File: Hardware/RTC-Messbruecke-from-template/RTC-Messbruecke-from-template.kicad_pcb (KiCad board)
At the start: 2 copper layers, 68.6 x 53.3 mm, 43 parts, among them J1 Power, J2 Digital/PWM, J3 Analog, J4 Digital/PWM, J5 Conn_01x04, J6 Conn_01x04, J7 Conn_01x08, J8 Conn_01x04, U1 R-78E9.0-0.5, U3 MAX6105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

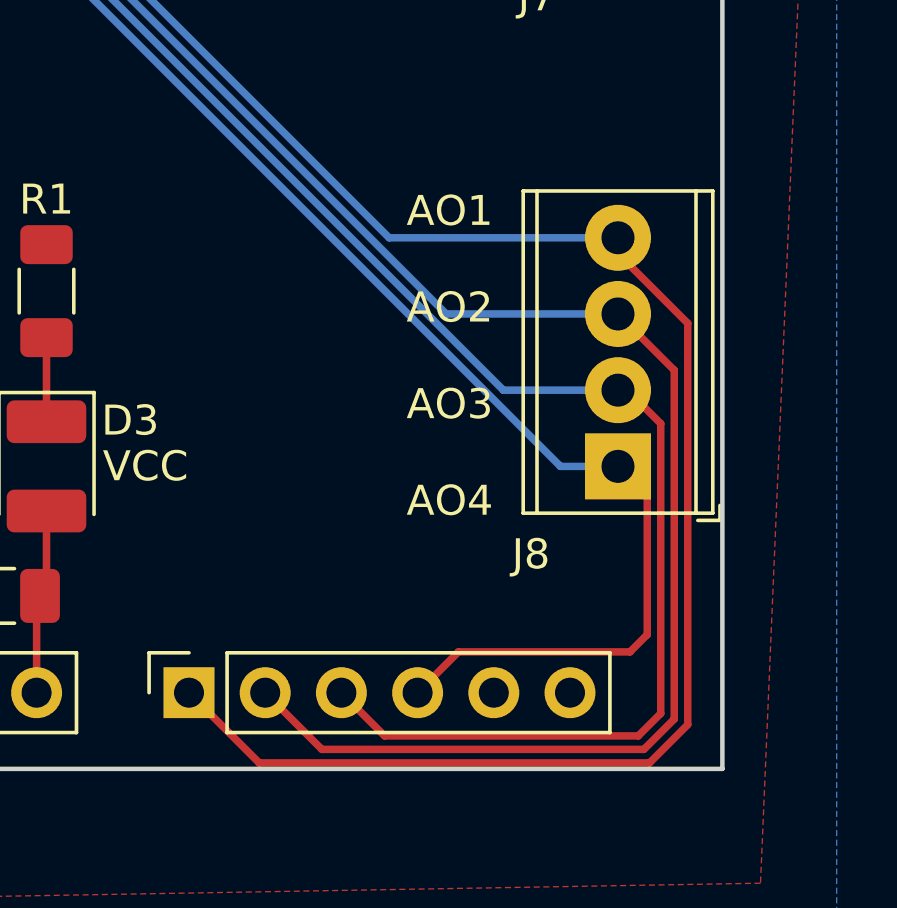
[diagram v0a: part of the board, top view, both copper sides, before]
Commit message: added test results and simulations
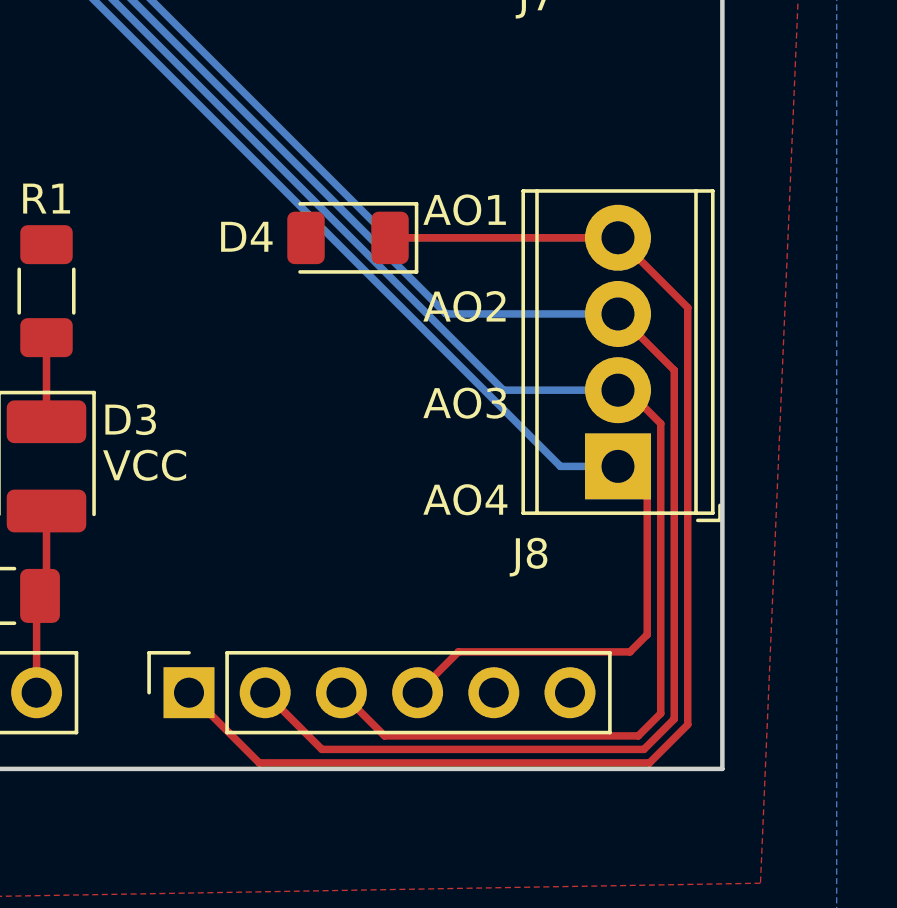
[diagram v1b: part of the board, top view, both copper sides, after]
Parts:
- added D4: D_Zener, Diode_SMD:D_1206_3216Metric, F.Cu at (156.1, 82.3)
- R21, R22, R25, R26, R31, R32, R35, R36: value 3k -> 10k
- R23, R27, R30, R34: value 1.28k -> 1k
- R24, R28, R29, R33: value 4.54k -> 22k
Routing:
- net /A0: track 80.4 -> 88.0 mm

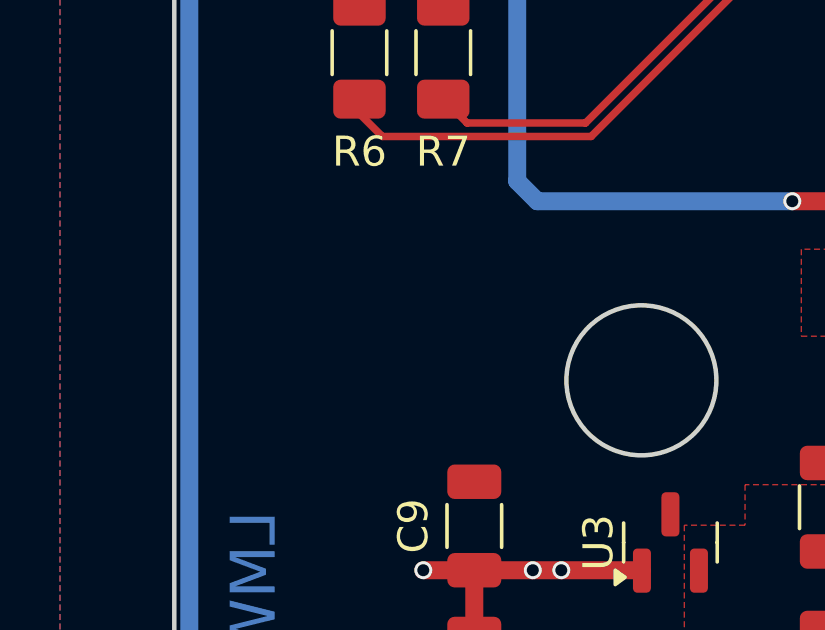
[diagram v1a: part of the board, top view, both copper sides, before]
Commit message: added REF-195 as alternativ voltage reference
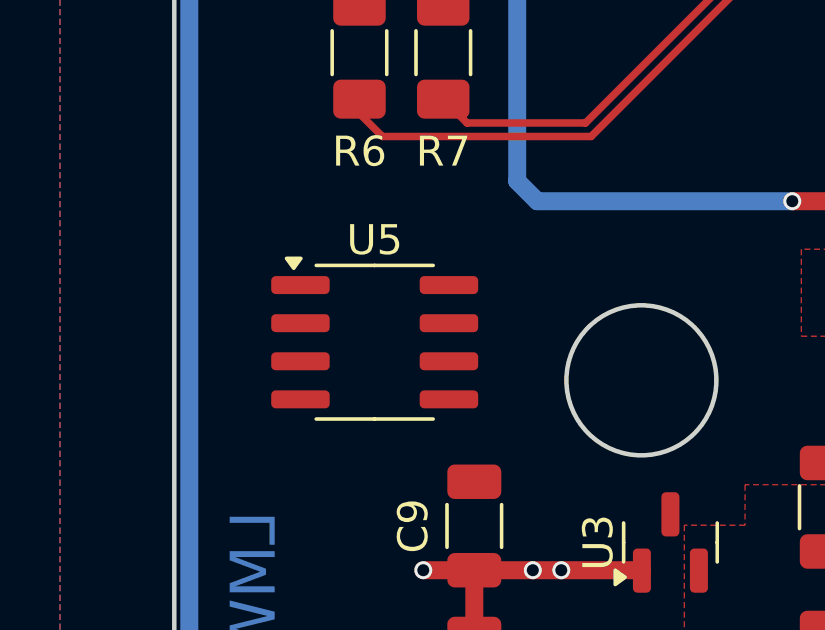
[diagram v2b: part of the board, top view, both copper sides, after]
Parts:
- added U5: REF195, Package_SO:SOIC-8_3.9x4.9mm_P1.27mm, F.Cu at (106.7, 63.5)
